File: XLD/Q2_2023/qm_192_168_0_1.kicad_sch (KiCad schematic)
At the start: 105 parts, among them T1 Terminator, T10 Terminator, T11 Terminator, T12 Terminator, T13 Terminator, T14 Terminator, T15 Terminator, T16 Terminator, T2 Terminator, T3 Terminator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

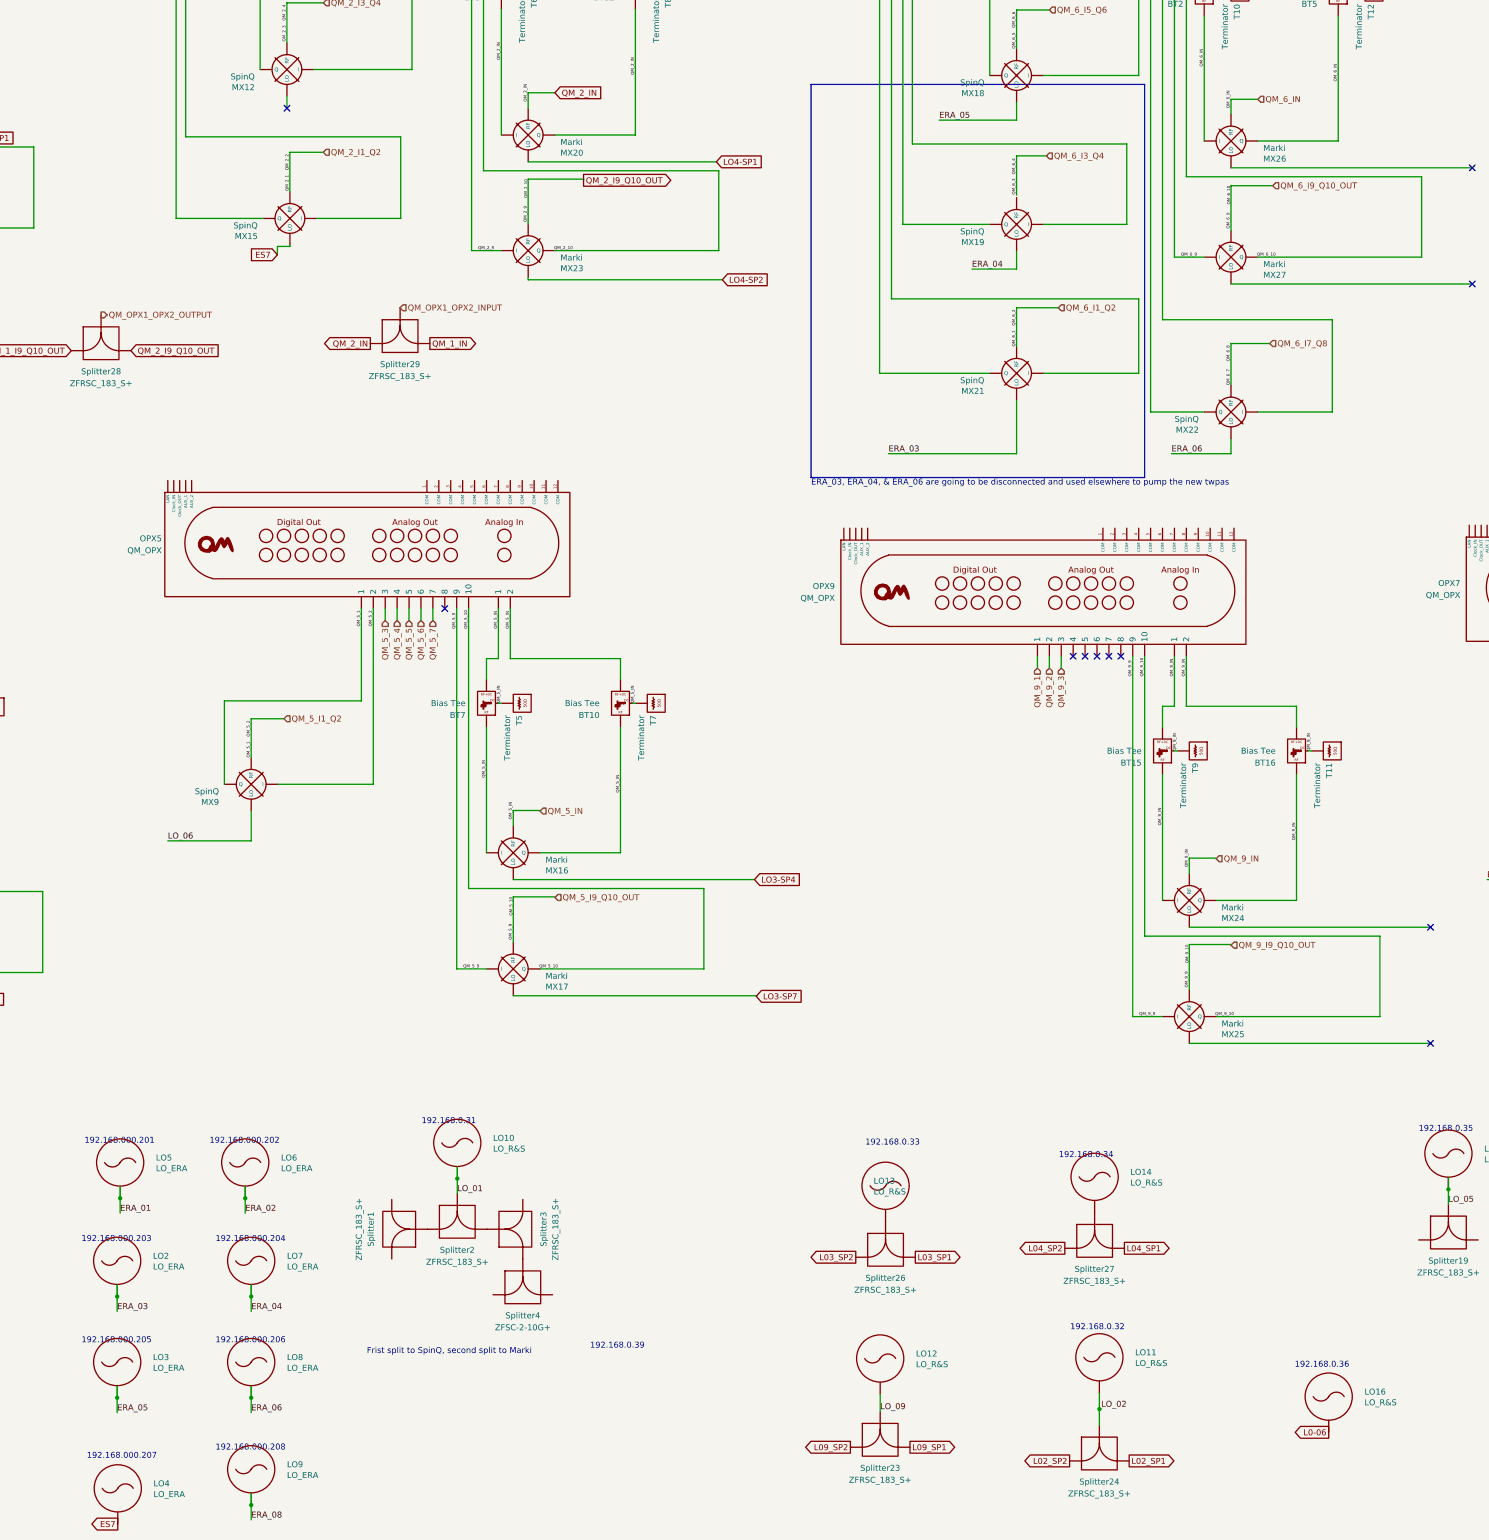
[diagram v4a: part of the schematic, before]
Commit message: organized labels
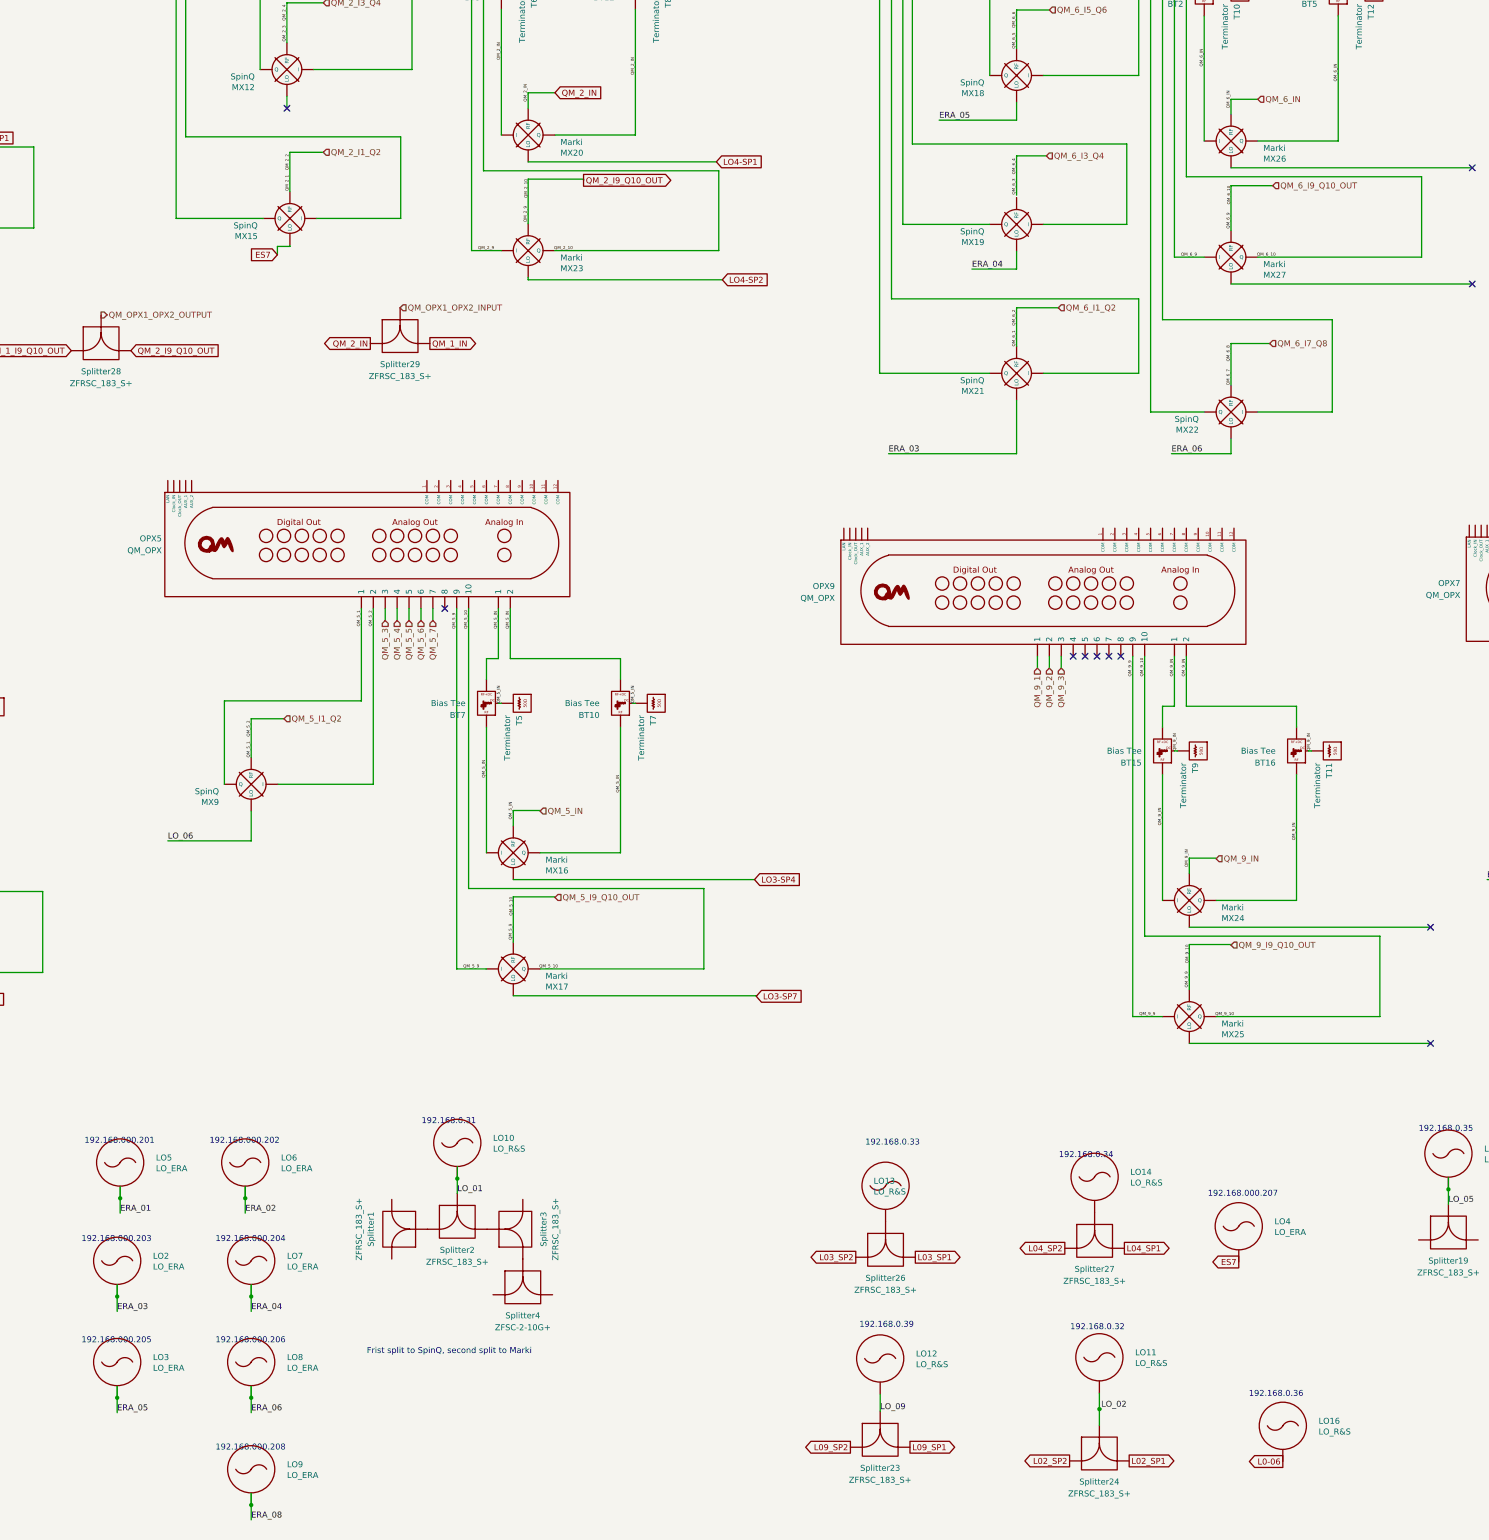
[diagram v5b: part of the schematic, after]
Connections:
- net at Splitter21.: now also Splitter20.
- net at Splitter22.: no longer Splitter21.
- net at Splitter20.: no longer Splitter21.
- net at Splitter1.: no longer Splitter2.
- net at Splitter3.: no longer Splitter2.
- net at Splitter4.: now also Splitter3.
- new net: Splitter21., Splitter22.
- new net: Splitter1., Splitter2.
- new net: Splitter2., Splitter3.
- now unconnected: Splitter3.
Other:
- note removed: "ERA_03, ERA_04, & ERA_06 are going to be disconnected and used elsewhere to pump the new twpas"
- moved on the sheet: LO16, LO4
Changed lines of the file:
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@@
     (stroke (width 0) (type default))
   )
-  (rectangle (start 307.34 93.345) (end 378.46 177.165)
-    (stroke (width 0) (type default))
-    (fill (type none))
-  )
   (text "192.168.000.208" (at 180.34 384.81 0)
     (effects (font (size 1.27 1.27)) (justify left bottom))
   )
-  (text "192.168.0.39" (at 260.223 363.093 0)
+  (text "192.168.0.39" (at 317.627 358.648 0)
     (effects (font (size 1.27 1.27)) (justify left bottom))
   )
@@
     (effects (font (size 1.27 1.27)) (justify left bottom))
   )
-  (text "192.168.000.207" (at 152.908 386.588 0)
+  (text "192.168.000.207" (at 391.922 330.708 0)
     (effects (font (size 1.27 1.27)) (justify left bottom))
   )
-  (text "192.168.0.36" (at 410.464 367.157 0)
+  (text "192.168.0.36" (at 400.685 373.38 0)
     (effects (font (size 1.27 1.27)) (justify left bottom))
   )
@@
     (effects (font (size 1.27 1.27)) (justify left bottom))
   )
-  (text "ERA_03, ERA_04, & ERA_06 are going to be disconnected and used elsewhere to pump the new twpas"
-    (at 307.34 179.07 0)
-    (effects (font (size 1.27 1.27)) (justify left bottom))
-  )
   (label "QM_6_10" (at 397.002 114.935 270) (fields_autoplaced)
     (effects (font (size 0.64 0.64)) (justify right bottom))
@@
     )
   )
-  (global_label "ES7" (shape output) (at 159.512 400.304 180) (fields_autoplaced)
+  (global_label "ES7" (shape output) (at 398.526 344.424 180) (fields_autoplaced)
     (effects (font (size 1.27 1.27)) (justify right))
-    (property "Intersheetrefs" "${INTERSHEET_REFS}" (at 152.9588 400.304 0)
+    (property "Intersheetrefs" "${INTERSHEET_REFS}" (at 391.9728 344.424 0)
       (effects (font (size 1.27 1.27)) (justify right) hide)
     )
@@
     )
   )
-  (global_label "L0-06" (shape output) (at 417.703 380.746 180) (fields_autoplaced)
+  (global_label "L0-06" (shape output) (at 407.924 386.969 180) (fields_autoplaced)
     (effects (font (size 1.27 1.27)) (justify right))
-    (property "Intersheetrefs" "${INTERSHEET_REFS}" (at 408.5682 380.746 0)
+    (property "Intersheetrefs" "${INTERSHEET_REFS}" (at 398.7892 386.969 0)
       (effects (font (size 1.27 1.27)) (justify right) hide)
     )
@@
     )
   )
-  (symbol (lib_id "Quantum Computing:LO_R&S") (at 417.703 373.126 0) (unit 1)
+  (symbol (lib_id "Quantum Computing:LO_R&S") (at 407.924 379.349 0) (unit 1)
     (in_bom yes) (on_board no) (dnp no) (fields_autoplaced)
-    (property "Reference" "LO16" (at 425.323 372.11 0)
+    (property "Reference" "LO16" (at 415.544 378.333 0)
       (effects (font (size 1.27 1.27)) (justify left))
     )
-    (property "Value" "LO_R&S" (at 425.323 374.396 0)
+    (property "Value" "LO_R&S" (at 415.544 380.619 0)
       (effects (font (size 1.27 1.27)) (justify left))
     )
-    (property "Footprint" "" (at 417.703 373.126 0)
+    (property "Footprint" "" (at 407.924 379.349 0)
       (effects (font (size 1.27 1.27)) hide)
     )
-    (property "Datasheet" "" (at 417.703 373.126 0)
+    (property "Datasheet" "" (at 407.924 379.349 0)
       (effects (font (size 1.27 1.27)) hide)
     )
@@
     )
   )
-  (symbol (lib_id "Quantum Computing:LO_ERA") (at 159.512 392.684 0) (unit 1)
+  (symbol (lib_id "Quantum Computing:LO_ERA") (at 398.526 336.804 0) (unit 1)
     (in_bom yes) (on_board no) (dnp no)
-    (property "Reference" "LO4" (at 167.132 391.668 0)
+    (property "Reference" "LO4" (at 406.146 335.788 0)
       (effects (font (size 1.27 1.27)) (justify left))
     )
-    (property "Value" "LO_ERA" (at 167.132 393.954 0)
+    (property "Value" "LO_ERA" (at 406.146 338.074 0)
       (effects (font (size 1.27 1.27)) (justify left))
     )
-    (property "Footprint" "" (at 159.512 392.684 0)
+    (property "Footprint" "" (at 398.526 336.804 0)
       (effects (font (size 1.27 1.27)) hide)
     )
-    (property "Datasheet" "" (at 159.512 392.684 0)
+    (property "Datasheet" "" (at 398.526 336.804 0)
       (effects (font (size 1.27 1.27)) hide)
     )

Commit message: removed lines for line C in qw25q
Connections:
- net at Splitter21.: now also Splitter20.
- net at Splitter22.: no longer Splitter21.
- net at Splitter20.: no longer Splitter21.
- net at Splitter1.: no longer Splitter2.
- net at Splitter3.: no longer Splitter2.
- net at Splitter4.: now also Splitter3.
- new net: Splitter21., Splitter22.
- new net: Splitter1., Splitter2.
- new net: Splitter2., Splitter3.
- now unconnected: Splitter3.
